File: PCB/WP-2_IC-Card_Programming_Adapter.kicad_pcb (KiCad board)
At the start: 2 copper layers, 85.1 x 59.4 mm, 21 parts, among them J1 TMS-138-01, J2 SST39SF020_DIP, J3 Conn_02x08_Odd_Even

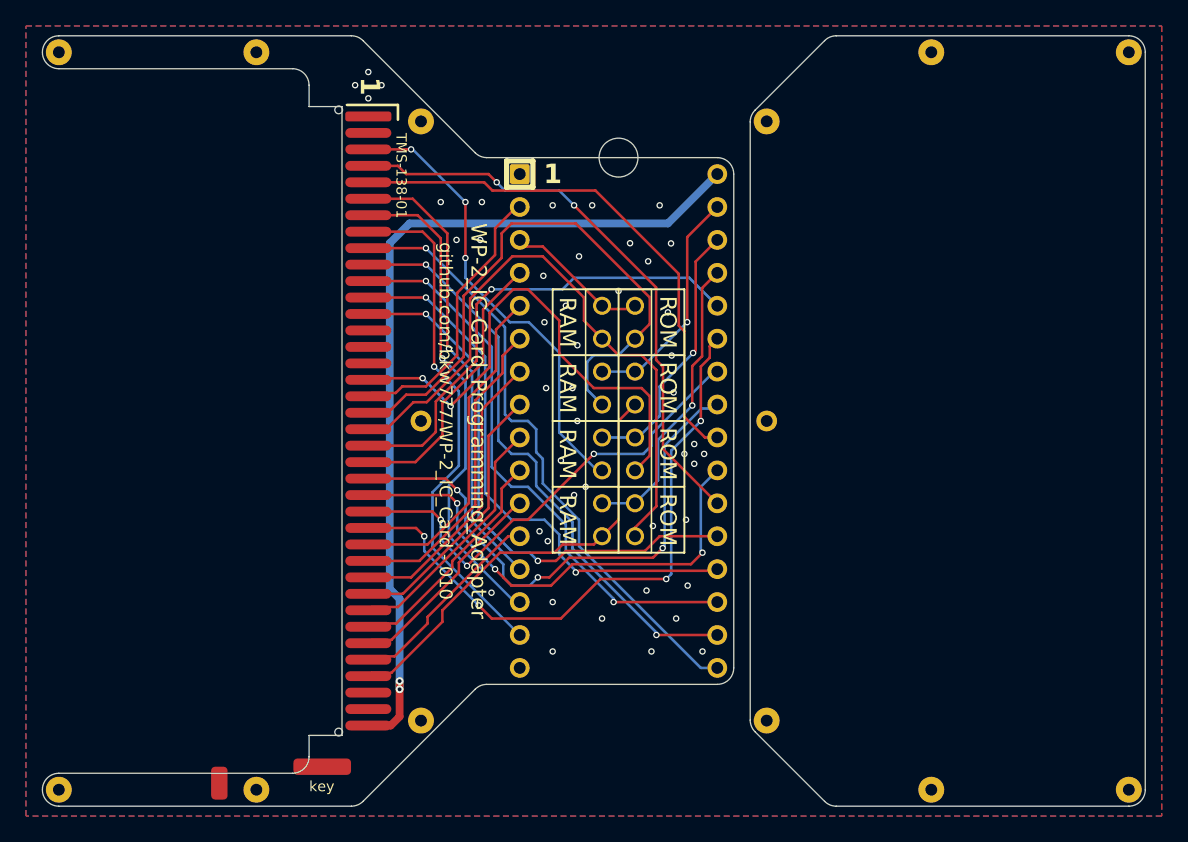
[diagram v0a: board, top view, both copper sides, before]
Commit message: programming adapter silkscreen
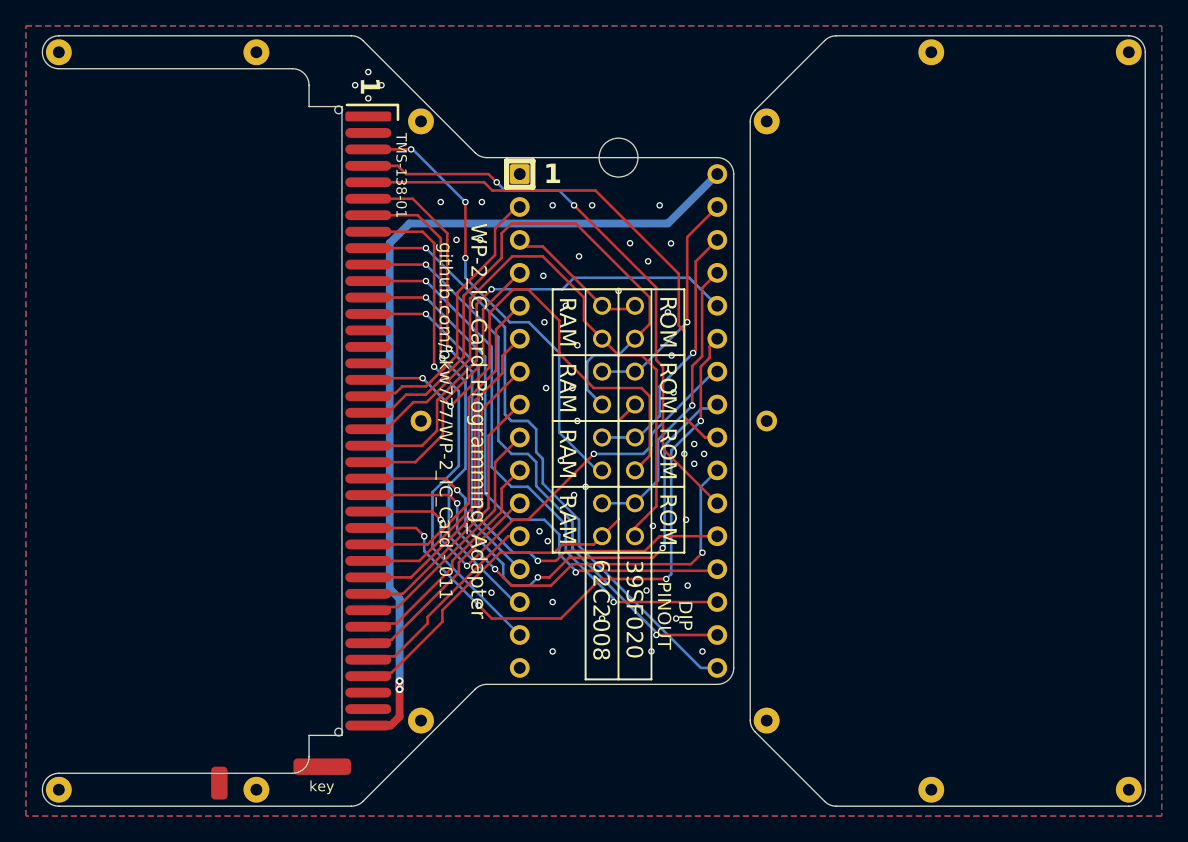
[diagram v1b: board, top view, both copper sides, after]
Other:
- board text added: "39SF020"
- board text added: "62C2008"
- board text added: "DIP PINOUT"

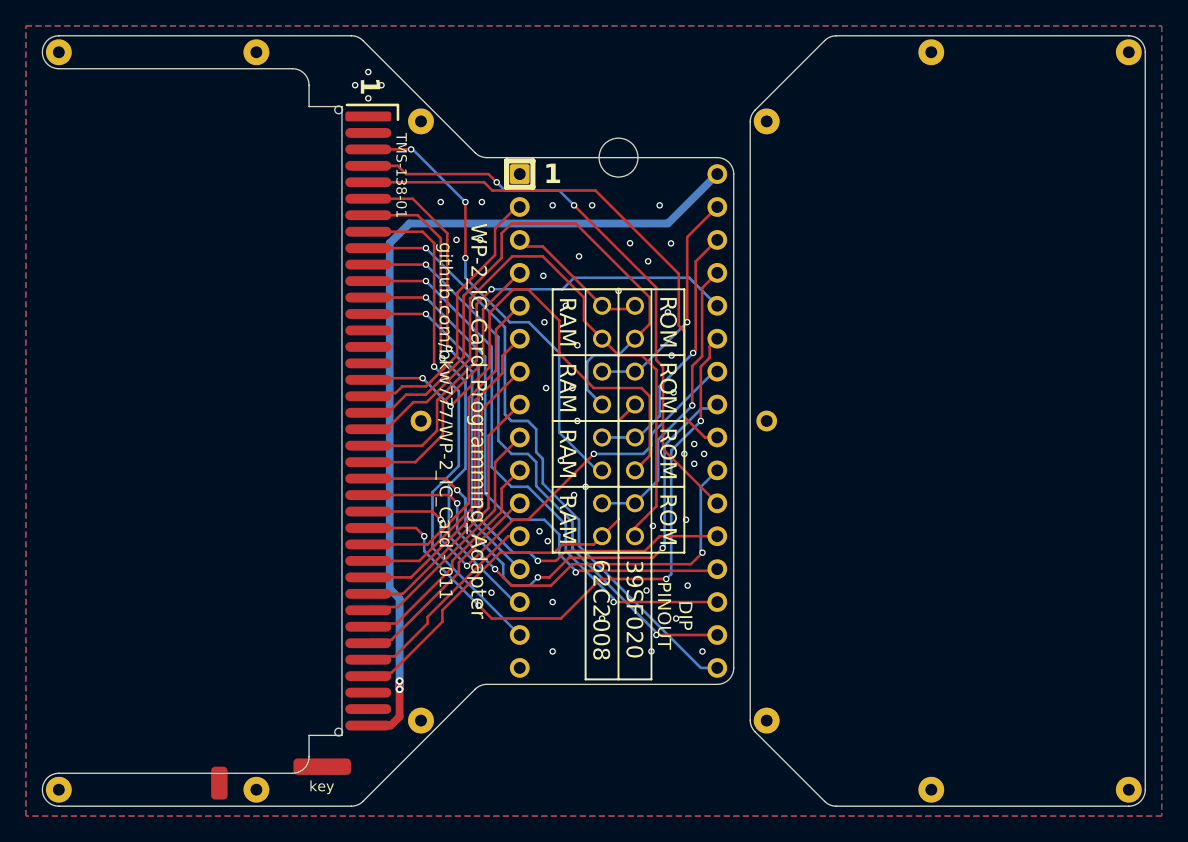
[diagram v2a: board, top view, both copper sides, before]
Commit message: bus tap & breakout minor adjustments
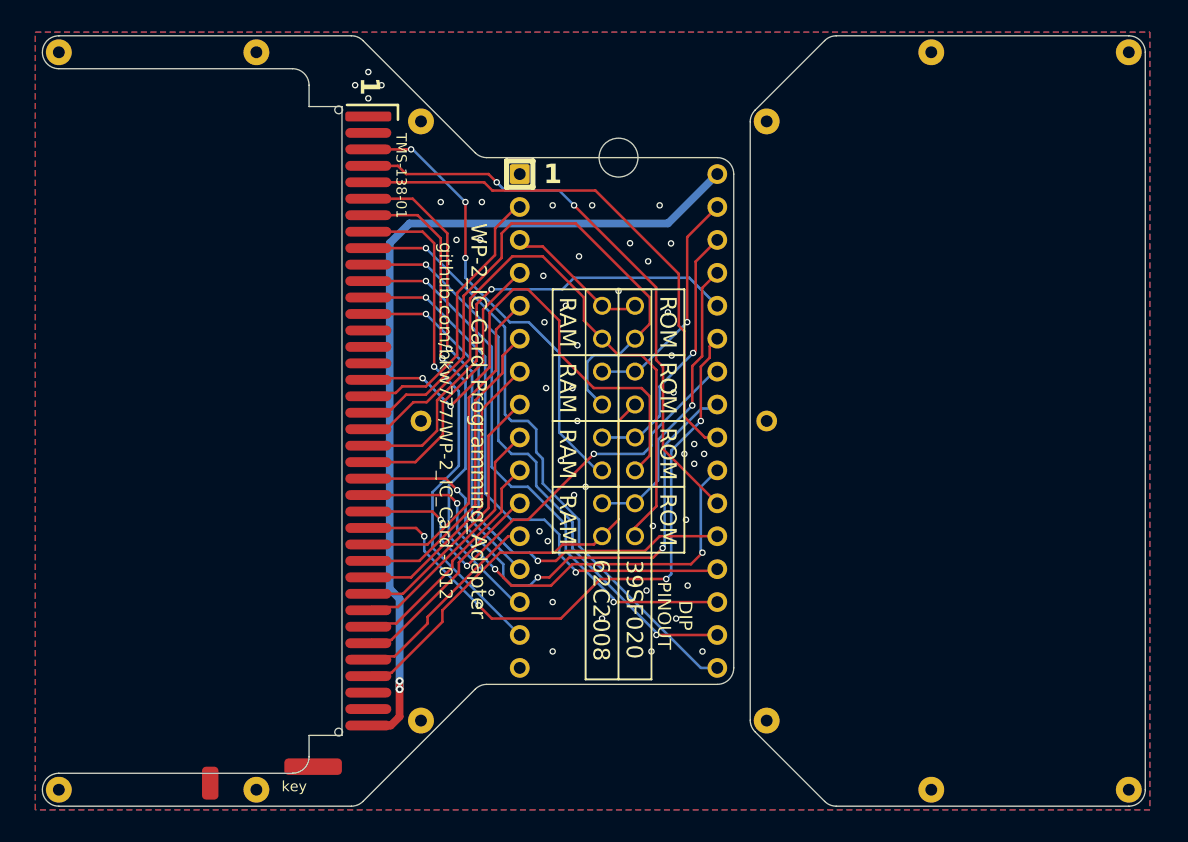
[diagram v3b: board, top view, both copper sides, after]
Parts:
- moved key 0.70 mm to (108.2, 118.7)
